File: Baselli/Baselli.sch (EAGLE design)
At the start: 60 parts, among them J2 DF12-ELLI-HEADER-TOP, J3 DF12-ELLI-RECEPTABLE-BOTTOM, J4 FTDI-SER-6-PP, J5 JTAG_PROG, Q1 MOSFET-PCHANNELIRLML2244, U1 LCMXO2-256HC-4SG32, U2 STM32F051R

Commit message: Small fixes to Baselli
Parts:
- SW1: value (none) -> A6H-2101
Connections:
- net DOUT: now also TP1.1; no longer TP1.P$1
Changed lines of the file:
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@@
 <part name="R30" library="ELL-i-Passives" deviceset="R" device="0805" value="180"/>
 <part name="R31" library="ELL-i-Passives" deviceset="R" device="0805" value="180"/>
-<part name="SW1" library="SparkFun-Electromechanical" deviceset="SW_DIP-2" device="-SMT-HALFSIZE"/>
+<part name="SW1" library="SparkFun-Electromechanical" deviceset="SW_DIP-2" device="-SMT-HALFSIZE" value="A6H-2101"/>
 </parts>
 <sheets>
@@
 <net name="DOUT" class="0">
 <segment>
-<pinref part="TP1" gate="TP$1" pin="P$1"/>
+<pinref part="TP1" gate="TP$1" pin="1"/>
 <pinref part="D1" gate="G$1" pin="DOUT"/>
 <wire x1="-88.9" y1="48.26" x2="-81.28" y2="48.26" width="0.1524" layer="91"/>

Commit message: Import fixed testpoints
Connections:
- net DOUT: now also TP1.P$1; no longer TP1.1
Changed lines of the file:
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@@
 <net name="DOUT" class="0">
 <segment>
-<pinref part="TP1" gate="TP$1" pin="1"/>
+<pinref part="TP1" gate="TP$1" pin="P$1"/>
 <pinref part="D1" gate="G$1" pin="DOUT"/>
 <wire x1="-88.9" y1="48.26" x2="-81.28" y2="48.26" width="0.1524" layer="91"/>

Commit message: BasElli review fixes
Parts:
- removed Y1: (no value), crystal:CRYSTALSM49
- added D4: BAS70J, ELL-i-DiscreteSemi:BAS70J
- added D5: BAT60J, SparkFun-DiscreteSemi:DIODE-SCHOTTKY-BAT60J
- added OLPADS1, OLPADS2: OUTLINE-PADS-10, ELL-i-Boards:OUTLINE-PADS-10
- added R32, R36, R37, R38, R39, R40, R41, R42, R43: NP, ELL-i-Passives:R0805
- added TP2, TP3, TP4, TP5: TEST_POINT-5000, ELL-i-Passives:TEST_POINT-5000
- added X1: 8MHz NP, SparkFun-FreqCtrl:CRYSTAL_WITH_GND
- DIMENSIONS1: value DIN49073 -> DIN49073-OUTLINE; device ELL-i-Boards:DIN49073 -> ELL-i-Boards:DIN49073-OUTLINE
- Q1: value MOSFET-PCHANNELIRLML2244 -> IRLML2244
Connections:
- removed net PA11-D3MCU: R31.1, U2PA.PA11
- removed net PB7-D8MCU: R30.1, U2PB.PB7
- new net N$1: R36.2, R43.2, U1PWR.VCCIO0
- new net N$2: R37.2, R40.2, U1PWR.VCCIO1
- new net N$3: R38.2, R41.2, U1PWR.VCCIO2
- new net N$4: R39.2, R42.2, U1PWR.VCCIO3
- new net N$5: R31.1, U2PB.PB8
- new net N$7: R30.1, U2PB.PB0-ADC_IN8
- net +3V3: now also D5.C, R36.1, R37.1, R38.1, R39.1, TP3.P$1; no longer U1PWR.VCCIO0, U1PWR.VCCIO1, U1PWR.VCCIO2, U1PWR.VCCIO3
- net +5V: now also TP4.P$1
- net AREF: now also J2.AREF
- net D3: now also U2PA.PA11; no longer R16.1, R31.2
- net D7: now also R16.1, R31.2; no longer U2PB.PB8
- net D8: now also U2PB.PB7; no longer R21.1, R30.2
- net D9: now also R21.1, R30.2; no longer U2PB.PB0-ADC_IN8
- net GNDI: now also TP2.P$1, X1.GND@2
- net N205481: now also X1.C1; no longer Y1.1
- net PF0: now also X1.C2; no longer Y1.2
- net PF7: now also R32.2
- net VBAT: now also D4.A, D4.C
- net VCC-IN: now also D5.A
- net VCCIO: now also R32.1, R40.1, R41.1, R42.1, R43.1, TP5.P$1
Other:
- note added: "Crystal circuit needs to be reviewed. Uncertainty about capacitor values etc."
- note added: "I2C pullup resistors"
- note added: "In STM32F072 TQFP64, PF6 and PF7 pins are used for GND and VCCIO"
- note removed: "Add a diode and connect VCC-IN to +5V or +3.3V in ELL-i bus?"
- note removed: "Connect one of the VCCIOs to ELL-i VCC(IO)?"
- note removed: "In STM32F072 TQFP100, PF6 and PF7 pins are used for GND and VCCIO"
- moved on the sheet: C4, C5, C6, C7, D1, D2, R1, R30, R31, TP1, U1PWR

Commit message: Baselli cleanups
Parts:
- removed R24, R25, R26, R27, R30, R31: 180, ELL-i-Passives:R0805
- removed R28, R29: 0, ELL-i-Passives:R0805
- removed R32, R36, R37, R38, R39, R40, R41, R42, R43: NP, ELL-i-Passives:R0805
- removed R33: 1k5, ELL-i-Passives:R0402
- removed R34, R35: 2K2, ELL-i-Passives:R0402
- added SJ1, SJ2, SJ3, SJ4: 1-2, SparkFun-Passives:SOLDERJUMPER_2WAYPASTE1&2
- added SJ10, SJ11, SJ12, SJ13, SJ14, SJ15, SJ16, SJ7, SJ8, SJ9: CLOSED, SparkFun-Passives:SOLDERJUMPERTRACE
- added SJ5, SJ6: OPEN, SparkFun-Passives:SOLDERJUMPERNO
- R10: value 0 -> 4K7 (NP); device ELL-i-Passives:R0402 -> ELL-i-Passives:R0603
- R11: value 0 -> 47K; device ELL-i-Passives:R0805 -> ELL-i-Passives:R0402
- R13: value NP -> 10k
- R14: value NP -> 180
- R15: value 10k -> 180
- R18, R19, R20, R21: value 0 -> 180
- R22: value 0 -> NP
- R23: value 0 -> 1k5; device ELL-i-Passives:R0805 -> ELL-i-Passives:R0402
- R4: value 47K -> 2K2
- R7: value 4K7 (NP) -> 2K2; device ELL-i-Passives:R0603 -> ELL-i-Passives:R0402
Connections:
- removed net JTAGENB$2: Q1.D, R11.2, R8.1, U1ERB.JTAGENB/PT15C
- removed net JTAGENB$3: J5.3, Q1.G, R4.2
- new net JTAGENB_MCU: SJ15.1, U2PB.PB4
- new net JTAGEN_GATE: J5.3, Q1.G, R11.2
- new net VBATT: D4.A, J2.VBATT, J3.VBATT
- net +3V3: now also R11.1, R7.1, SJ1.1, SJ16.2, SJ2.1, SJ3.1, SJ4.1, SJ5.1; no longer R10.2, R12.1, R34.1, R35.1, R36.1, R37.1, R38.1, R39.1
- net A4: now also R7.2; no longer R5.2
- net AREF: now also R13.2; no longer R15.2
- net BOOT0: now also R23.2; no longer R33.2
- net D7: now also R15.2, SJ14.1; no longer R16.1, R31.2
- net D9: now also R14.2, SJ9.1; no longer R21.1, R30.2
- net DONE: now also SJ14.2; no longer R16.2
- net E0: now also R18.2, SJ10.1; no longer R20.1, R27.2
- net E1: now also R19.2, SJ11.1; no longer R19.1, R26.2
- net E12: now also R17.2, R5.2, SJ7.1; no longer R23.1, R28.2, R34.2
- net E13: now also R16.2, R4.2, SJ8.1; no longer R22.1, R29.2, R35.2
- net E2: now also R20.2, SJ12.1; no longer R18.1, R25.2
- net E3: now also R21.2, SJ13.1; no longer R17.1, R24.2
- net GNDI: now also R10.2, R12.1, R23.1, SJ6.1, X1.GND@1; no longer R13.1, R14.1, R33.1, R7.2
- net JTAGENB: now also Q1.D, R8.1, SJ15.2, U1ERB.JTAGENB/PT15C; no longer R11.1, U2PB.PB4
- net N$1: now also SJ4.2; no longer R36.2, R43.2
- net N$10: now also SJ11.2; no longer R19.2
- net N$12: now also SJ9.2; no longer R21.2
- net N$15: now also SJ12.2; no longer R18.2
- net N$16: now also SJ13.2; no longer R17.2
- net N$17: now also SJ7.2; no longer R23.2
- net N$2: now also SJ3.2; no longer R37.2, R40.2
- net N$20: now also SJ8.2; no longer R22.2
- net N$3: now also SJ2.2; no longer R38.2, R41.2
- net N$4: now also SJ1.2; no longer R39.2, R42.2
- net N$5: now also R15.1; no longer R31.1
- net N$6: now also R12.2; no longer R14.2
- net N$7: now also R14.1; no longer R30.1
- net N$9: now also SJ10.2; no longer R20.2
- net PB10: now also R16.1; no longer R29.1
- net PB11: now also R17.1; no longer R28.1
- net PF4: now also R18.1; no longer R27.1
- net PF5: now also R19.1; no longer R26.1
- net PF6: now also R20.1, SJ6.2; no longer R13.2, R25.1
- net PF7: now also R21.1, R22.2, SJ5.2; no longer R12.2, R24.1, R32.2
- net SWCLK: now also R10.1; no longer R7.1
- net VBAT: no longer D4.A, J2.VBATT, J3.VBATT
- net VCCIO: now also R22.1, SJ1.3, SJ16.1, SJ2.3, SJ3.3, SJ4.3; no longer R10.1, R32.1, R40.1, R41.1, R42.1, R43.1
- net VDDA: now also R13.1; no longer R15.1
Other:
- note added: "Real time oscillator missing!"
- moved on the sheet: D2, D4, R1, R10, R11, R12, R13, R14, R15, R16, R17, R18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

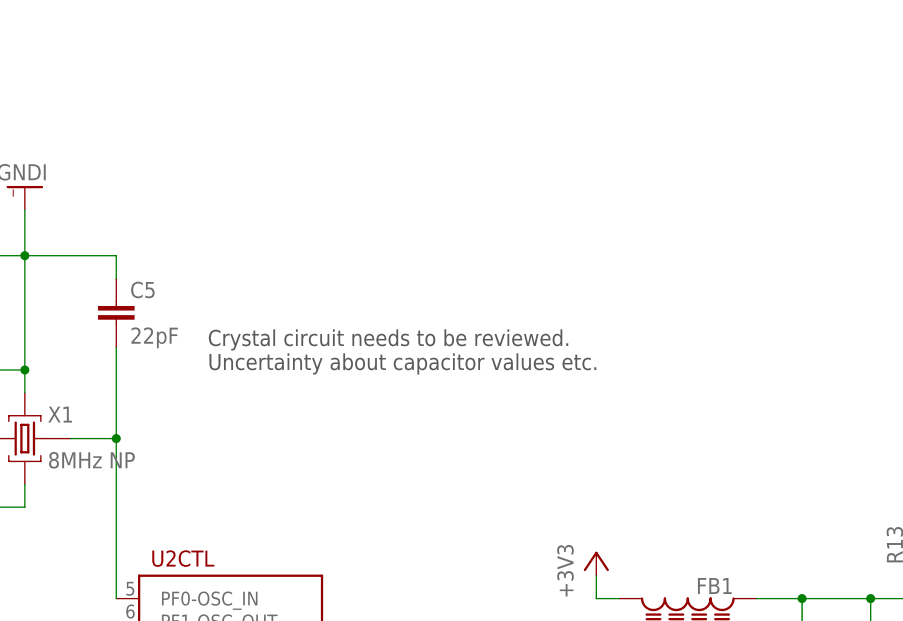
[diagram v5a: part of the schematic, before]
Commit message: Add rtc crystal
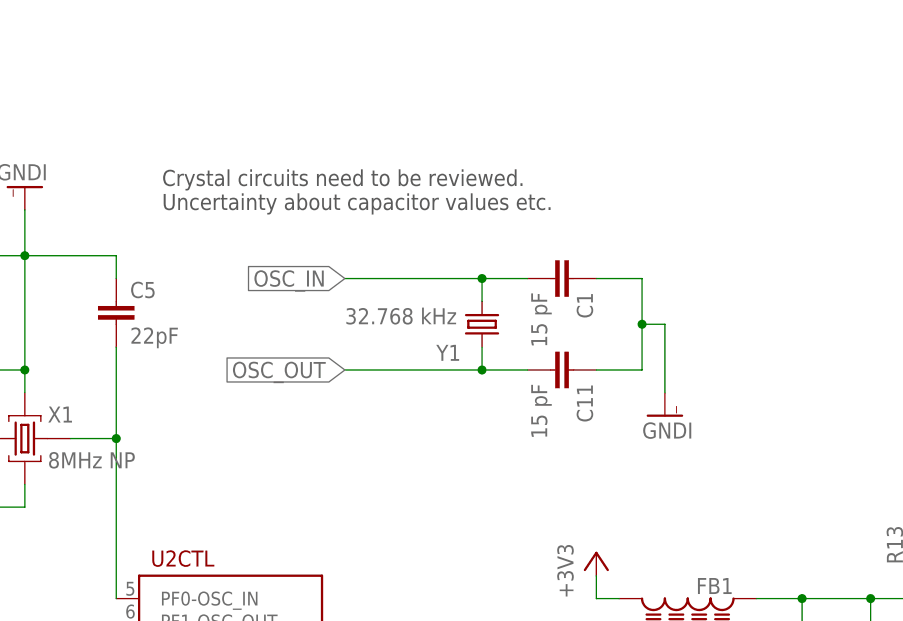
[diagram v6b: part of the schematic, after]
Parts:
- added C1, C11: 15 pF, ELL-i-Passives:C0402
- added Y1: 32.768 kHz, SparkFun-FreqCtrl:CRYSTAL32-SMD
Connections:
- new net OSC_IN: C1.2, Y1.1
- new net OSC_OUT: C11.2, Y1.2
- net GNDI: now also C1.1, C11.1
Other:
- note added: "Crystal circuits need to be reviewed. Uncertainty about capacitor values etc."
- note removed: "Crystal circuit needs to be reviewed. Uncertainty about capacitor values etc."
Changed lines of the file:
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@@
 <part name="R15" library="ELL-i-Passives" deviceset="R" device="0805" value="180"/>
 <part name="R14" library="ELL-i-Passives" deviceset="R" device="0805" value="180"/>
+<part name="Y1" library="SparkFun-FreqCtrl" deviceset="CRYSTAL" device="32-SMD" value="32.768 kHz"/>
+<part name="C1" library="ELL-i-Passives" deviceset="C" device="0402" value="15 pF"/>
+<part name="C11" library="ELL-i-Passives" deviceset="C" device="0402" value="15 pF"/>
+<part name="GNDI17" library="supply1" deviceset="GNDI" device=""/>
 </parts>
 <sheets>
@@
 GND and
 VCCIO</text>
-<text x="-177.8" y="154.94" size="1.778" layer="97">Crystal circuit needs to be reviewed.
+<text x="-182.88" y="172.72" size="1.778" layer="97">Crystal circuits need to be reviewed.
 Uncertainty about capacitor values etc.</text>
 <text x="2.54" y="83.82" size="1.778" layer="97" rot="R90">I2C pullup resistors</text>
@@
 <instance part="R15" gate="G$1" x="119.38" y="104.14"/>
 <instance part="R14" gate="G$1" x="119.38" y="124.46"/>
+<instance part="Y1" gate="G$1" x="-147.32" y="160.02" smashed="yes" rot="R270">
+<attribute name="NAME" x="-152.4" y="155.956" size="1.778" layer="95"/>
+<attribute name="VALUE" x="-162.56" y="160.02" size="1.778" layer="96"/>
+</instance>
+<instance part="C1" gate="G$1" x="-137.16" y="165.1" rot="R270"/>
+<instance part="C11" gate="G$1" x="-137.16" y="154.94" rot="R270"/>
+<instance part="GNDI17" gate="G$1" x="-127" y="149.86"/>
 </instances>
 <busses>
@@
 <wire x1="-35.56" y1="35.56" x2="-35.56" y2="33.02" width="0.1524" layer="91"/>
 </segment>
+<segment>
+<pinref part="C1" gate="G$1" pin="1"/>
+<wire x1="-134.62" y1="165.1" x2="-129.54" y2="165.1" width="0.1524" layer="91"/>
+<pinref part="C11" gate="G$1" pin="1"/>
+<wire x1="-134.62" y1="154.94" x2="-129.54" y2="154.94" width="0.1524" layer="91"/>
+<wire x1="-129.54" y1="154.94" x2="-129.54" y2="160.02" width="0.1524" layer="91"/>
+<wire x1="-129.54" y1="160.02" x2="-129.54" y2="165.1" width="0.1524" layer="91"/>
+<wire x1="-129.54" y1="160.02" x2="-127" y2="160.02" width="0.1524" layer="91"/>
+<junction x="-129.54" y="160.02"/>
+<wire x1="-127" y1="160.02" x2="-127" y2="152.4" width="0.1524" layer="91"/>
+<pinref part="GNDI17" gate="G$1" pin="GNDI"/>
+</segment>
 </net>
 <net name="A0" class="0">
@@
 </segment>
 </net>
+<net name="OSC_OUT" class="0">
+<segment>
+<pinref part="C11" gate="G$1" pin="2"/>
+<pinref part="Y1" gate="G$1" pin="2"/>
+<wire x1="-142.24" y1="154.94" x2="-147.32" y2="154.94" width="0.1524" layer="91"/>
+<wire x1="-147.32" y1="154.94" x2="-147.32" y2="157.48" width="0.1524" layer="91"/>
+<wire x1="-147.32" y1="154.94" x2="-162.56" y2="154.94" width="0.1524" layer="91"/>
+<junction x="-147.32" y="154.94"/>
+<label x="-162.56" y="154.94" size="1.778" layer="95" rot="R180" xref="yes"/>
+</segment>
+</net>
+<net name="OSC_IN" class="0">
+<segment>
+<pinref part="C1" gate="G$1" pin="2"/>
+<pinref part="Y1" gate="G$1" pin="1"/>
+<wire x1="-142.24" y1="165.1" x2="-147.32" y2="165.1" width="0.1524" layer="91"/>
+<wire x1="-147.32" y1="165.1" x2="-147.32" y2="162.56" width="0.1524" layer="91"/>
+<wire x1="-147.32" y1="165.1" x2="-162.56" y2="165.1" width="0.1524" layer="91"/>
+<junction x="-147.32" y="165.1"/>
+<label x="-162.56" y="165.1" size="1.778" layer="95" rot="R180" xref="yes"/>
+</segment>
+</net>

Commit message: Small fixes to Baselli
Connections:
- net +3V3: now also C6.1, C7.1, C8.1, C9.1, J2.ETH_MUX, J3.ETH_MUX; no longer C6.2, C7.2, C8.2, C9.2
- net AREF: now also R13.1; no longer R13.2
- net BOOT0TX: now also R3.2; no longer R3.1
- net D0: now also R3.1; no longer R3.2
- net D7: now also R15.1; no longer R15.2
- net D9: now also R14.1; no longer R14.2
- net E13: now also R16.1; no longer R16.2
- net GNDI: now also C4.2, C6.2, C7.2, C8.2, C9.2, FB2.2, R8.1; no longer C4.1, C6.1, C7.1, C8.1, C9.1, FB2.1, J2.ETH_MUX, J3.ETH_MUX, R8.2
- net JTAGENB: now also R8.2; no longer R8.1
- net N$5: now also R15.2; no longer R15.1
- net N$7: now also R14.2; no longer R14.1
- net N205481: now also C4.1; no longer C4.2
- net PB10: now also R16.2; no longer R16.1
- net VDDA: now also C2.1, C3.1, R13.2; no longer C2.2, C3.2, R13.1
- net VSSA: now also C2.2, C3.2, FB2.1; no longer C2.1, C3.1, FB2.2

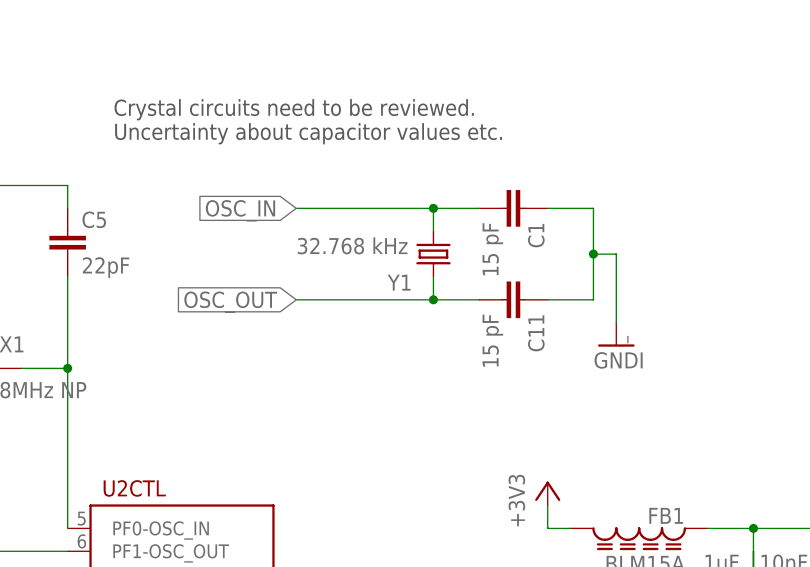
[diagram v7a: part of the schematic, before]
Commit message: Add 32 kHz oscillator to .brd & rename
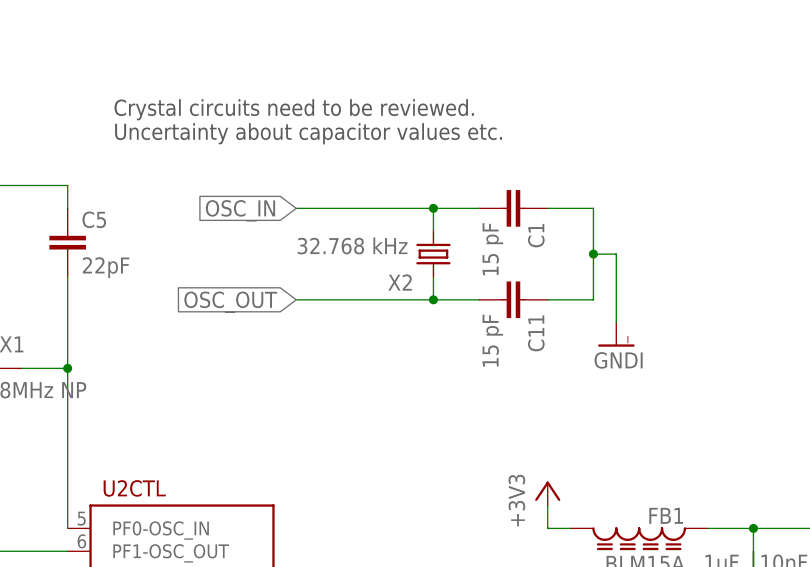
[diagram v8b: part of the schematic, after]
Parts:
- renumbered Y1 to X2
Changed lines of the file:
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@@
 <part name="R15" library="ELL-i-Passives" deviceset="R" device="0805" value="180"/>
 <part name="R14" library="ELL-i-Passives" deviceset="R" device="0805" value="180"/>
-<part name="Y1" library="SparkFun-FreqCtrl" deviceset="CRYSTAL" device="32-SMD" value="32.768 kHz"/>
+<part name="X2" library="SparkFun-FreqCtrl" deviceset="CRYSTAL" device="32-SMD" value="32.768 kHz"/>
 <part name="C1" library="ELL-i-Passives" deviceset="C" device="0402" value="15 pF"/>
 <part name="C11" library="ELL-i-Passives" deviceset="C" device="0402" value="15 pF"/>
@@
 <instance part="R15" gate="G$1" x="119.38" y="104.14"/>
 <instance part="R14" gate="G$1" x="119.38" y="124.46"/>
-<instance part="Y1" gate="G$1" x="-147.32" y="160.02" smashed="yes" rot="R270">
+<instance part="X2" gate="G$1" x="-147.32" y="160.02" smashed="yes" rot="R270">
 <attribute name="NAME" x="-152.4" y="155.956" size="1.778" layer="95"/>
 <attribute name="VALUE" x="-162.56" y="160.02" size="1.778" layer="96"/>
@@
 <segment>
 <pinref part="C11" gate="G$1" pin="2"/>
-<pinref part="Y1" gate="G$1" pin="2"/>
+<pinref part="X2" gate="G$1" pin="2"/>
 <wire x1="-142.24" y1="154.94" x2="-147.32" y2="154.94" width="0.1524" layer="91"/>
 <wire x1="-147.32" y1="154.94" x2="-147.32" y2="157.48" width="0.1524" layer="91"/>
@@
 <segment>
 <pinref part="C1" gate="G$1" pin="2"/>
-<pinref part="Y1" gate="G$1" pin="1"/>
+<pinref part="X2" gate="G$1" pin="1"/>
 <wire x1="-142.24" y1="165.1" x2="-147.32" y2="165.1" width="0.1524" layer="91"/>
 <wire x1="-147.32" y1="165.1" x2="-147.32" y2="162.56" width="0.1524" layer="91"/>
